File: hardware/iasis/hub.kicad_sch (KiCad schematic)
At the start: 57 parts, among them U201 USB7206CT/KDX, U204 SN74AUP1G08DCKR, Y201 X322525MSB4SI

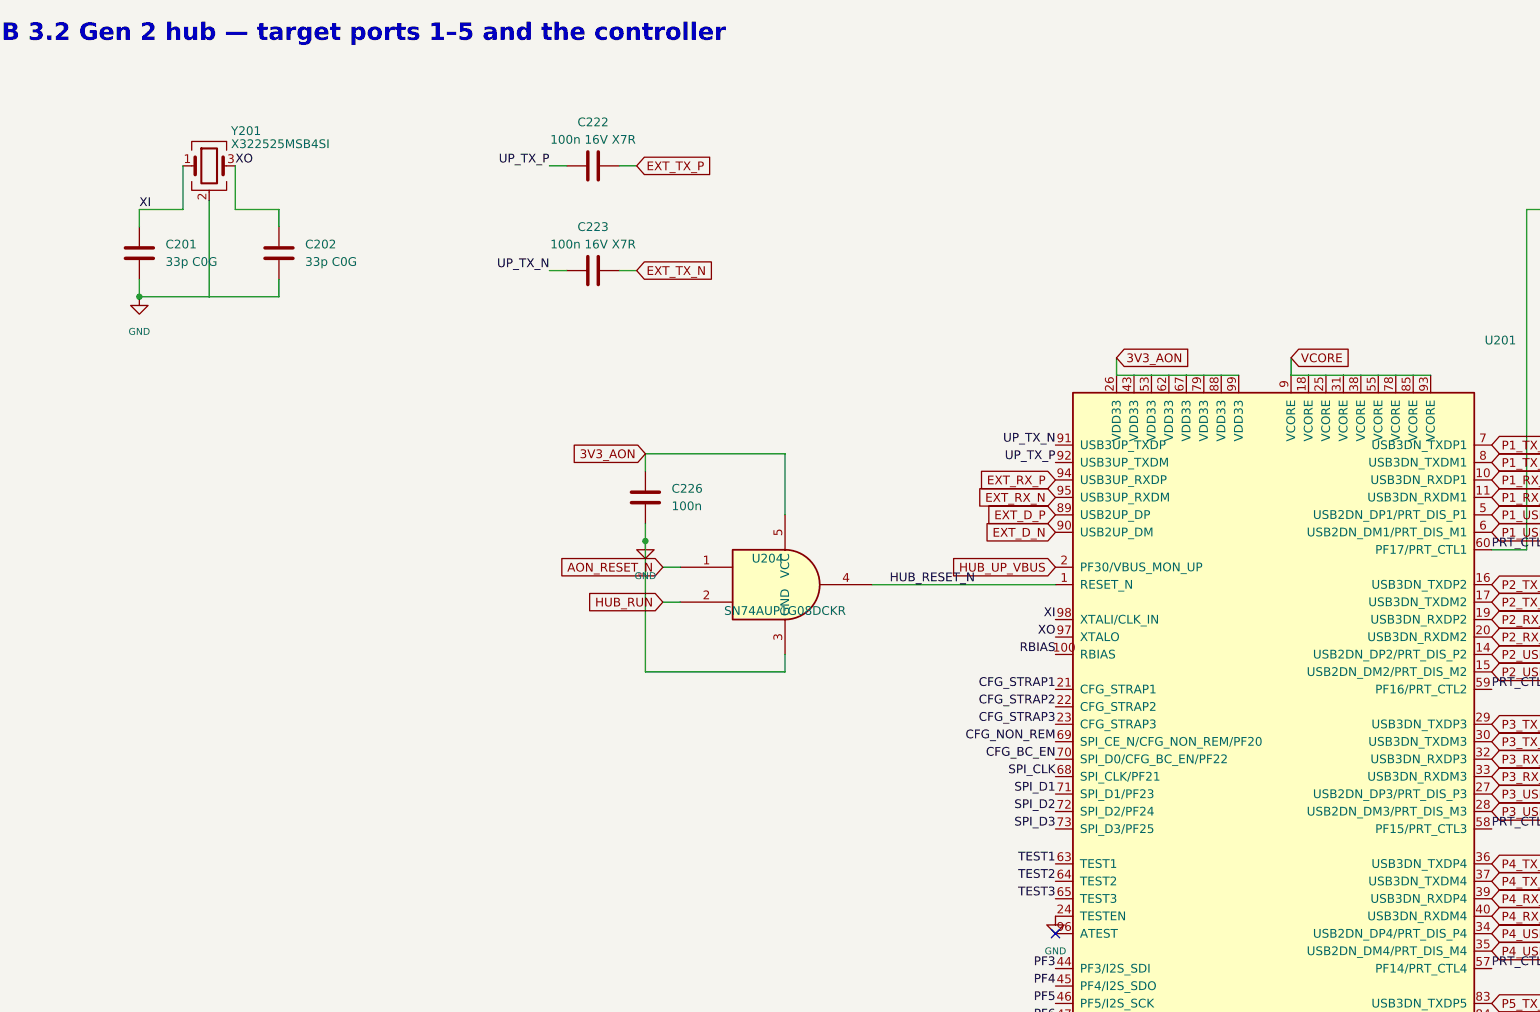
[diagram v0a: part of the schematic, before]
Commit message: Wire the schematic islands and side-match the RP2354 GPIOs
Each sheet now draws its circuits with wires. Labels remain at block edges
and on single-part islands: buttons, test points, decoupling and pull
resistors. The target-port page wires its hierarchical labels straight to
the child sheet pins, the ports page points its labels away from each
block, and the root sheet keeps every block clear of the title block.

The RP2354B GPIOs are reassigned so each signal leaves the package on the
side facing its destination. Update PCB from Schematic applied the 43
U1101 pad-net changes with no geometry change. Otherwise the netlist
matches the previous design, ERC keeps its 14 existing warnings and DRC
reports no parity issues.
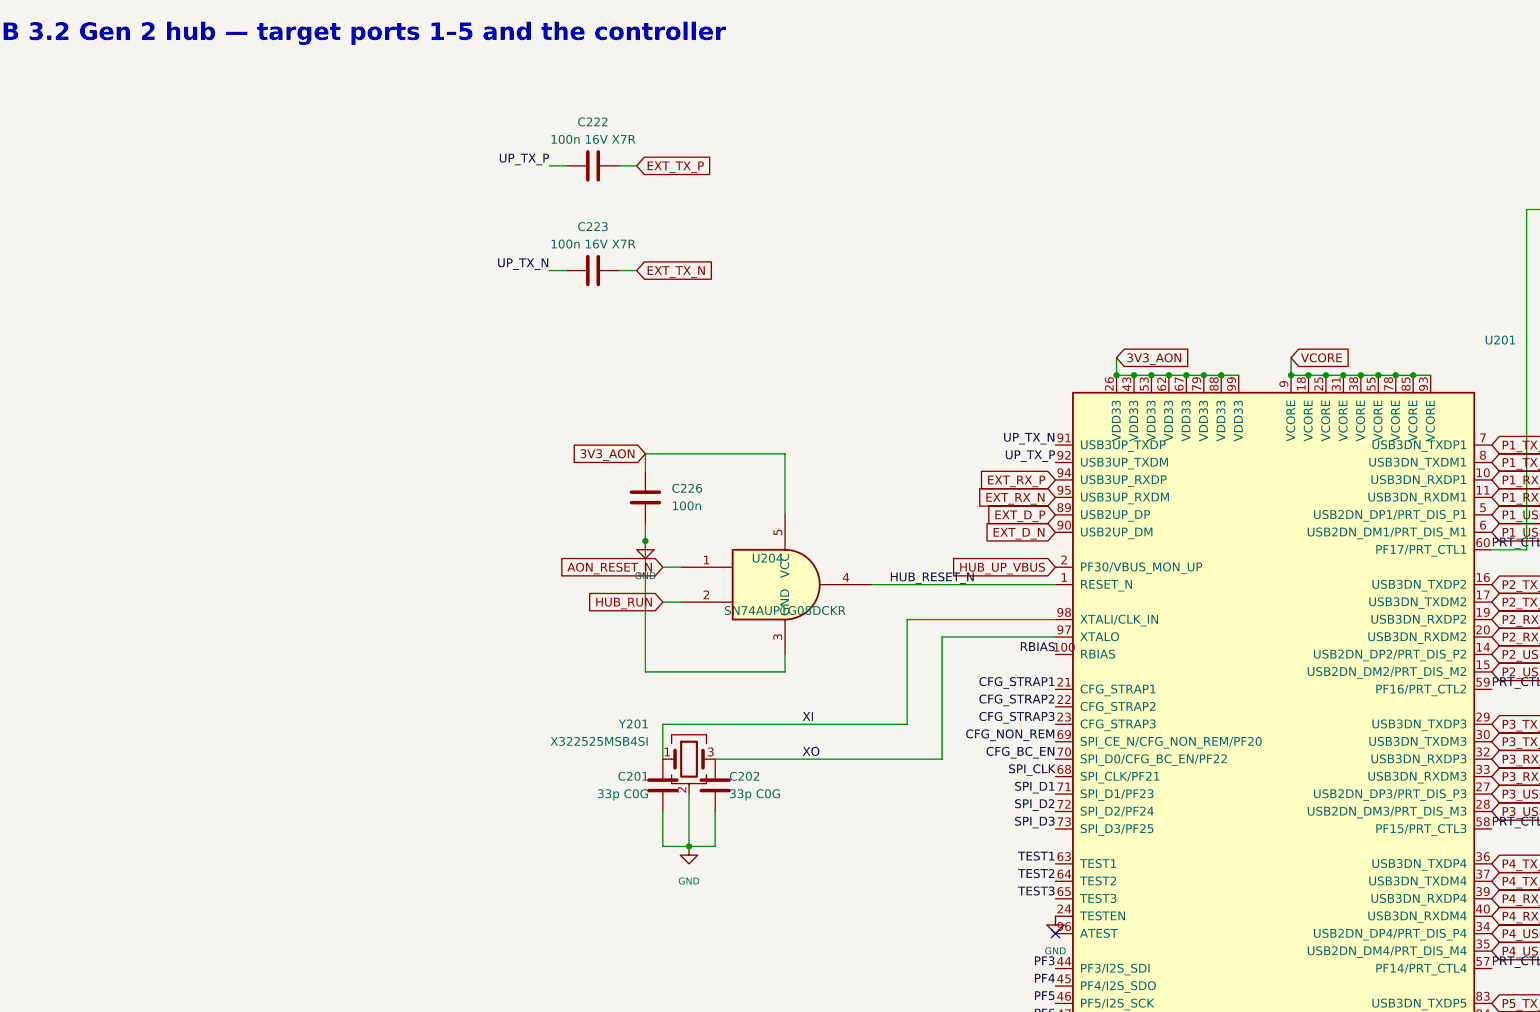
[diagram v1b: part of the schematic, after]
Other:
- moved on the sheet: C201, C202, Y201

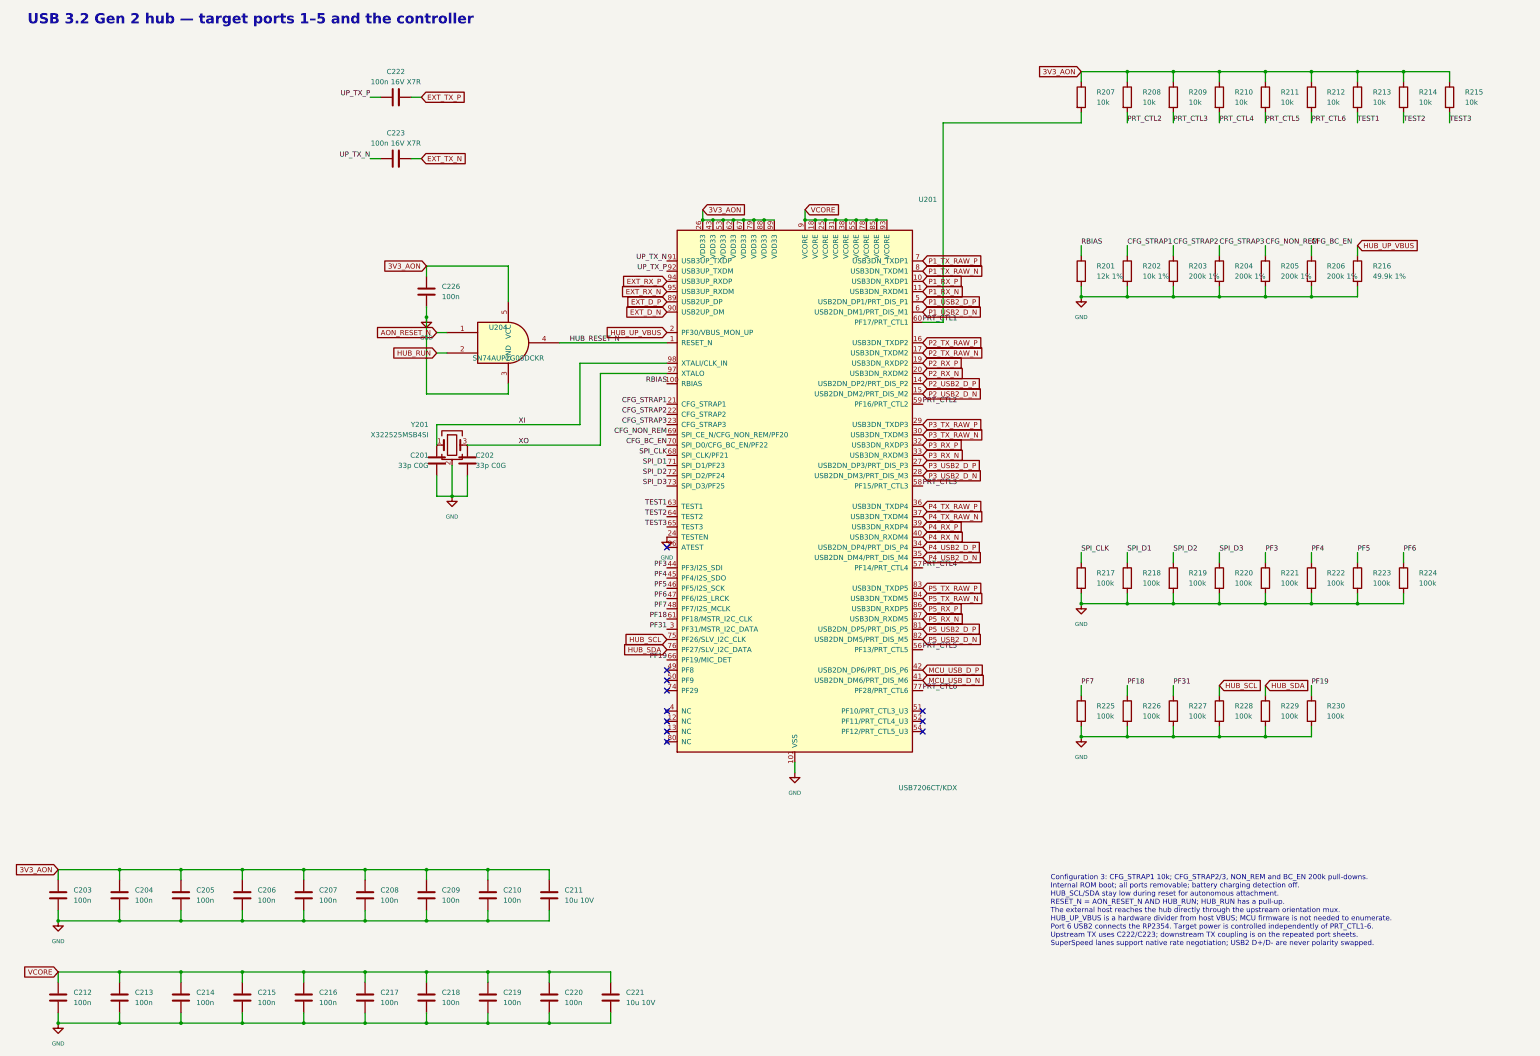
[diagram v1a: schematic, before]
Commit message: Redraw the host port and hub sheets
The host port mirrors the target data sheet. On the hub sheet the
VDD33 and VCORE pins tie to rails above the chip with their decoupling
on each rail, the crystal hangs under XI and XO, and the strap and
port-control resistors stand in banks on GND and 3V3_AON.

The USB7206C symbol's supply pins move up 2.54 mm so their names clear
the corner pin names. Pin numbers and electrical types are unchanged,
and the netlist is unchanged.
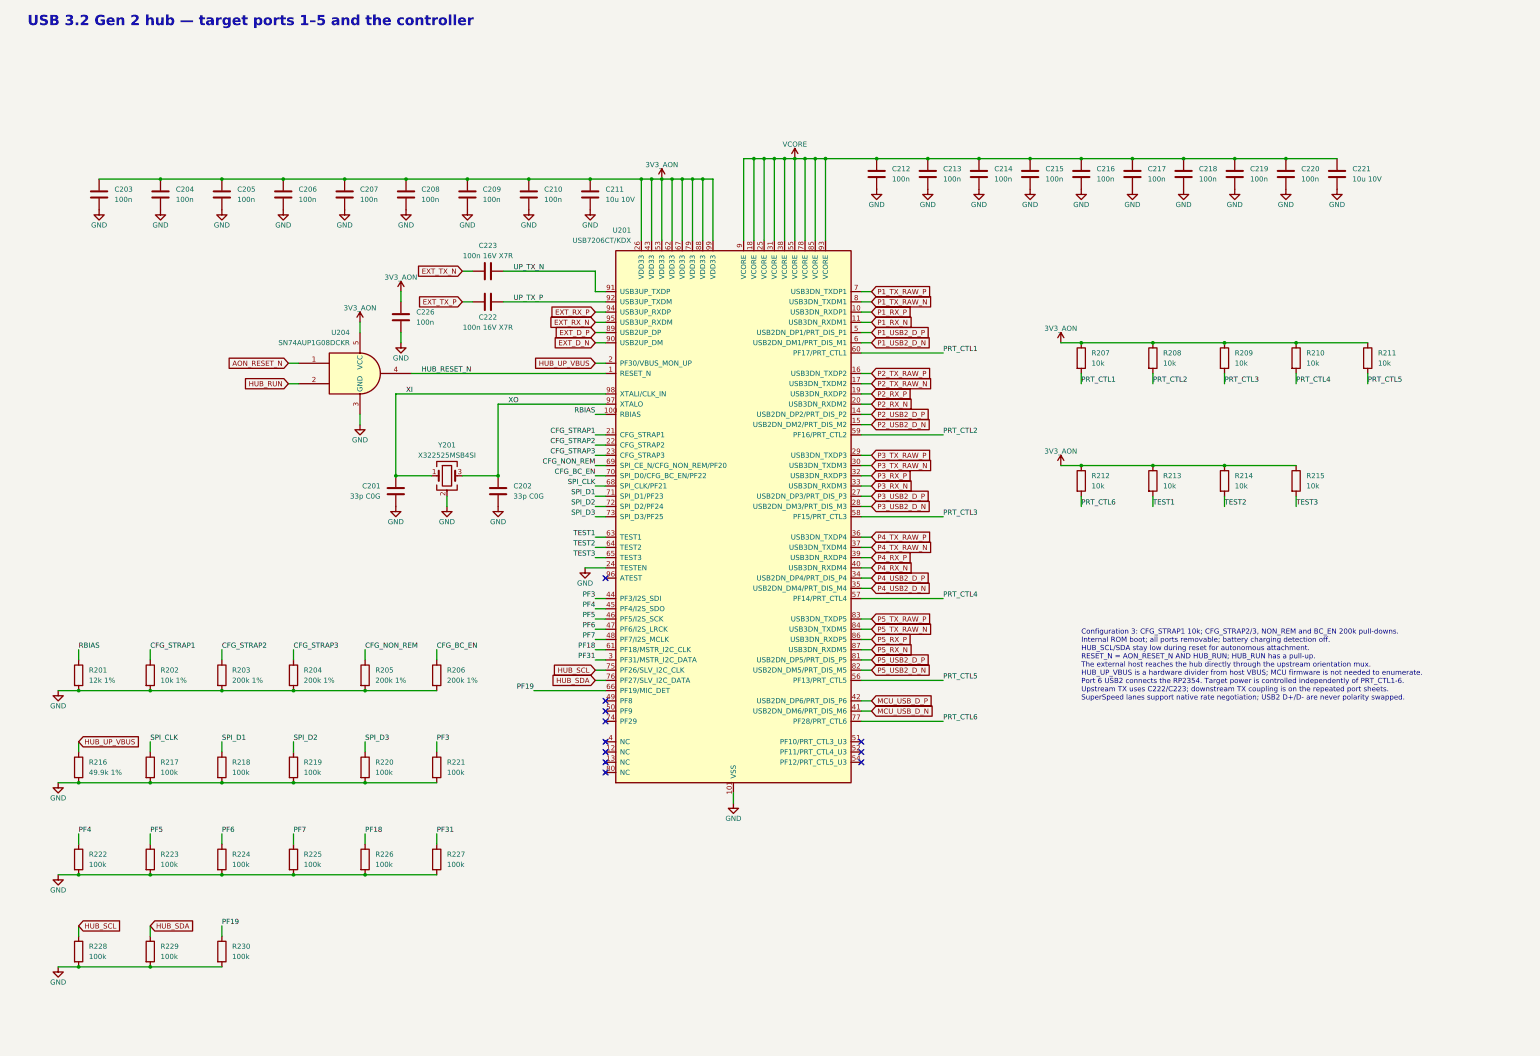
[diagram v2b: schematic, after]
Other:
- title: (none) -> USB 3.2 Gen 2 hub — target ports 1–5 and the controller
- moved on the sheet: C201, C202, C203, C204, C205, C206, C207, C208, C209, C210, C211, C212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

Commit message: Drill every via and thermal via at 0.3 mm
JLC prices 0.2 and 0.25 mm holes as a small-via tier that also forces
TG155 and a 4-wire Kelvin test: $39.18 on a five-board order. With
every plated hole at 0.3 mm or more the board quotes in the standard
tier.

- 2,005 vias keep their pads (0.45, 0.55, 0.6 mm) and drill 0.3 mm.
- U201's VQFN-100, the WQFN-20 and the HTSSOP-16 ThermalVias
  footprints move to Iasis.pretty copies with 0.3 mm thermal vias
  (121 holes); the schematic links follow.
- Rules match JLC's published via limits: 0.2 mm via hole to copper
  and hole to hole, 0.075 mm annular ring, 0.3 mm minimum hole.

DRC with refill and parity: 0 errors, 0 warnings, 0 unconnected.
Pour island counts unchanged; ERC unchanged at 14.
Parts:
- U201: footprint Package_DFN_QFN:VQFN-100-1EP_12x12mm_P0.4mm_EP8x8mm_ThermalVias -> Iasis:VQFN-100-1EP_12x12mm_P0.4mm_EP8x8mm_ThermalVias
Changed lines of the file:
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@@
 			)
 		)
-		(property "Footprint" "Package_DFN_QFN:VQFN-100-1EP_12x12mm_P0.4mm_EP8x8mm_ThermalVias"
+		(property "Footprint" "Iasis:VQFN-100-1EP_12x12mm_P0.4mm_EP8x8mm_ThermalVias"
 			(at 200.66 142.24 0)
 			(hide yes)

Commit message: Fit YAGEO RC0402FR-0749K9L as R216
JLC stock of 0402WGF4992TCE (C25897) fell from 1,208 to 8 this
evening, short of the 20 an order buys. YAGEO RC0402FR-0749K9L
(C137969, 1,338,801 in stock) has the same rating: 49.9 kΩ ±1 %,
±100 ppm/°C, 62.5 mW, 0402 thick film.

R216 changes LCSC, MPN, Manufacturer and Datasheet only. Netlist
connectivity identical (651 components, 541 nets). ERC 14 as before.
DRC with refill and parity: 0 errors, 0 warnings, 0 unconnected.
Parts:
- R216: LCSC C25897 -> C137969; MPN 0402WGF4992TCE -> RC0402FR-0749K9L; Manufacturer UNI-ROYAL(Uniroyal Elec) -> YAGEO
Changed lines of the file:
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@@
 			)
 		)
-		(property "Datasheet" "https://www.lcsc.com/datasheet/lcsc_datasheet_2206010045_UNI-ROYAL-Uniroyal-Elec-0402WGF4992TCE_C25897.pdf"
+		(property "Datasheet" "https://www.lcsc.com/datasheet/lcsc_datasheet_2304140030_YAGEO-RC0402FR-0749K9L_C137969.pdf"
 			(at 38.1 207.01 0)
 			(hide yes)
@@
 			)
 		)
-		(property "LCSC" "C25897"
+		(property "LCSC" "C137969"
 			(at 38.1 207.01 0)
 			(hide yes)
@@
 			)
 		)
-		(property "MPN" "0402WGF4992TCE"
+		(property "MPN" "RC0402FR-0749K9L"
 			(at 38.1 207.01 0)
 			(hide yes)
@@
 			)
 		)
-		(property "Manufacturer" "UNI-ROYAL(Uniroyal Elec)"
+		(property "Manufacturer" "YAGEO"
 			(at 38.1 207.01 0)
 			(hide yes)

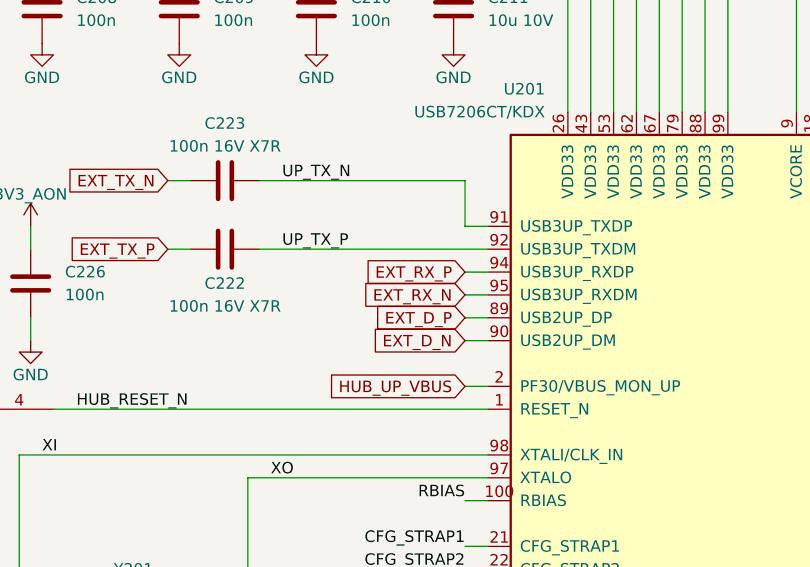
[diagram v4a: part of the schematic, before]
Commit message: Route the USB lanes
Every SuperSpeed, USB 2 and MCU USB pair now runs from the hub to its port,
the host connector or the controller, length-matched within each pair and
with ground return vias at the layer changes. Hub pins 94/95 take EXT_RX_N/P
so the upstream receive pair needs no crossing; the hub's receiver corrects
lane polarity.
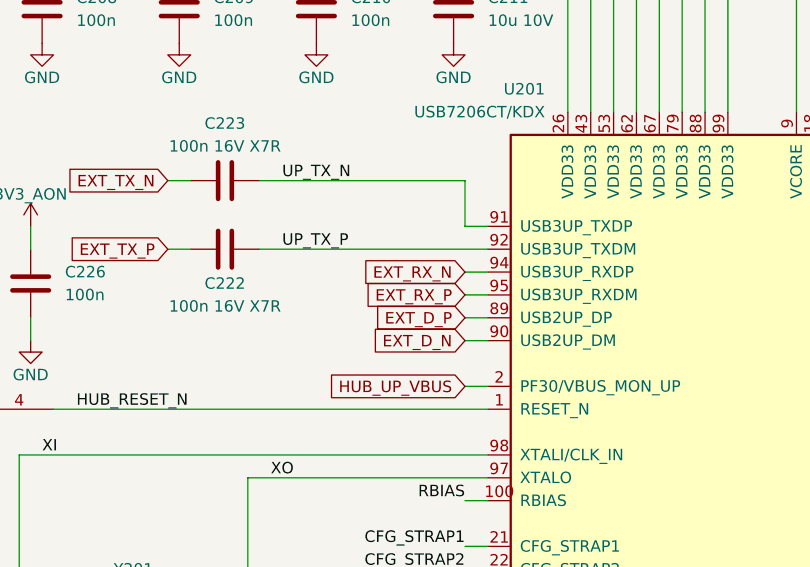
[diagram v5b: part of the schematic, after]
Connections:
- net EXT_RX_N: now also U201.94 (USB3UP_RXDP); no longer U201.95 (USB3UP_RXDM)
- net EXT_RX_P: now also U201.95 (USB3UP_RXDM); no longer U201.94 (USB3UP_RXDP)
